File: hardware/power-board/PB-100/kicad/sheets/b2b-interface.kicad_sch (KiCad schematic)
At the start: 1 part

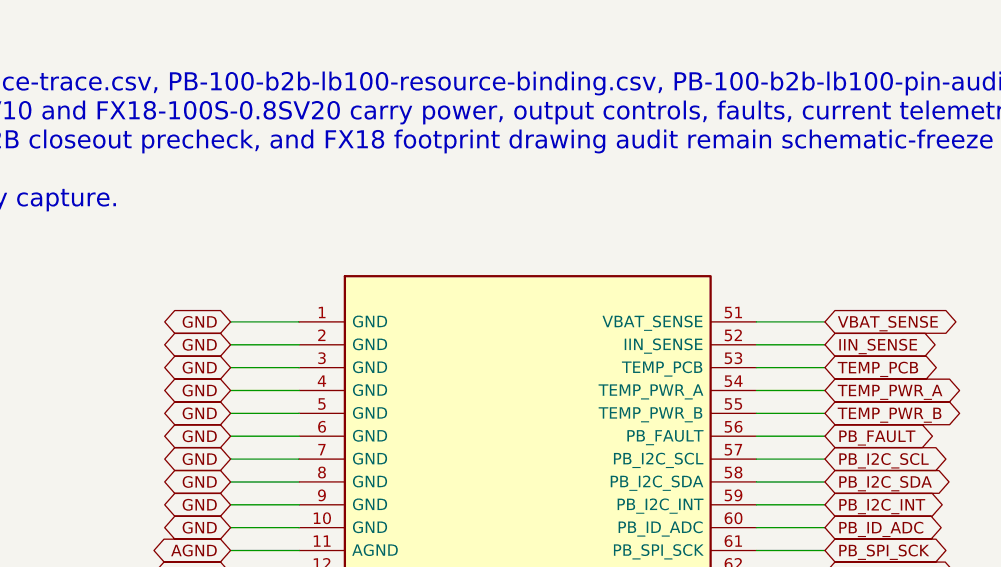
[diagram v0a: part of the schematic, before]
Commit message: feat(hardware): accept CAN1 and 80V freeze decisions
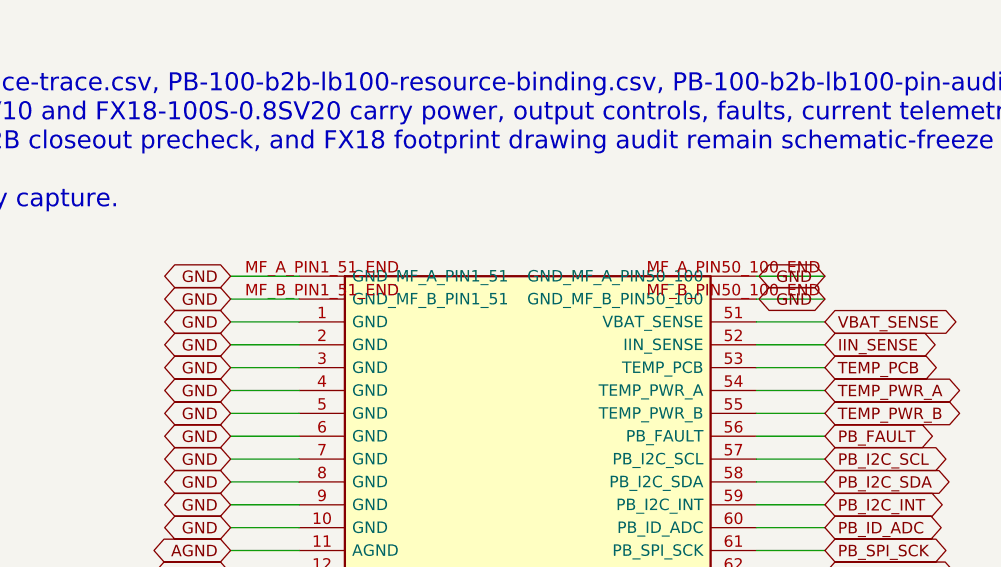
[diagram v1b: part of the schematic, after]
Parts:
- JPB1: footprint (none) -> PB100:FX18-100P-0.8SV10_Hirose
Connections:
- net GND: now also JPB1.MF_A_PIN1_51_END (GND_MF_A_PIN1_51), JPB1.MF_A_PIN50_100_END (GND_MF_A_PIN50_100), JPB1.MF_B_PIN1_51_END (GND_MF_B_PIN1_51), JPB1.MF_B_PIN50_100_END (GND_MF_B_PIN50_100)
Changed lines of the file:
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@@
     (property "Reference" "JPB1" (at 127.00 106.68 0) (effects (font (size 1.27 1.27))))
     (property "Value" "JPB1_100PIN_PRELIM" (at 127.00 109.22 0) (effects (font (size 1.27 1.27))))
-    (property "Footprint" "" (at 127.00 121.92 0) (effects (font (size 1.27 1.27)) hide))
+    (property "Footprint" "PB100:FX18-100P-0.8SV10_Hirose" (at 127.00 121.92 0) (effects (font (size 1.27 1.27)) hide))
     (property "Datasheet" "../PB-100-schematic-capture-plan.md" (at 127.00 124.46 0) (effects (font (size 1.27 1.27)) hide))
     (pin "1")
@@
     (pin "99")
     (pin "100")
+    (pin "MF_A_PIN1_51_END")
+    (pin "MF_B_PIN1_51_END")
+    (pin "MF_A_PIN50_100_END")
+    (pin "MF_B_PIN50_100_END")
     (instances
       (project "PB-100"
@@
     )
   )
+  (wire (pts (xy 101.60 45.72) (xy 93.98 45.72)) (stroke (width 0) (type default)))
+  (global_label "GND" (shape bidirectional) (at 93.98 45.72 0) (fields_autoplaced) (effects (font (size 1.27 1.27)) (justify right)) (property "Intersheetrefs" "${INTERSHEET_REFS}" (at 93.98 45.72 0) (effects (font (size 1.27 1.27)) hide)))
+  (wire (pts (xy 101.60 48.26) (xy 93.98 48.26)) (stroke (width 0) (type default)))
+  (global_label "GND" (shape bidirectional) (at 93.98 48.26 0) (fields_autoplaced) (effects (font (size 1.27 1.27)) (justify right)) (property "Intersheetrefs" "${INTERSHEET_REFS}" (at 93.98 48.26 0) (effects (font (size 1.27 1.27)) hide)))
+  (wire (pts (xy 152.40 45.72) (xy 160.02 45.72)) (stroke (width 0) (type default)))
+  (global_label "GND" (shape bidirectional) (at 160.02 45.72 180) (fields_autoplaced) (effects (font (size 1.27 1.27)) (justify right)) (property "Intersheetrefs" "${INTERSHEET_REFS}" (at 160.02 45.72 0) (effects (font (size 1.27 1.27)) hide)))
+  (wire (pts (xy 152.40 48.26) (xy 160.02 48.26)) (stroke (width 0) (type default)))
+  (global_label "GND" (shape bidirectional) (at 160.02 48.26 180) (fields_autoplaced) (effects (font (size 1.27 1.27)) (justify right)) (property "Intersheetrefs" "${INTERSHEET_REFS}" (at 160.02 48.26 0) (effects (font (size 1.27 1.27)) hide)))
   (wire (pts (xy 101.60 50.80) (xy 93.98 50.80)) (stroke (width 0) (type default)))
   (global_label "GND" (shape bidirectional) (at 93.98 50.80 0) (fields_autoplaced) (effects (font (size 1.27 1.27)) (justify right)) (property "Intersheetrefs" "${INTERSHEET_REFS}" (at 93.98 50.80 0) (effects (font (size 1.27 1.27)) hide)))

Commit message: feat(hardware): close LB FB schematics and FX18 mechanics
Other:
- note added: "B2B interface capture notes: - Source traces: PB-100-b2b-interface-trace.csv, PB-100-b2b-lb100-resource-binding.csv, PB-100-b2b-lb100-pin-audit-checklist.csv, PB-100-b2b-interface-freeze-checklist.csv, PB-100-b2b-interface-closeout-precheck.csv, PB-100-b2b-pin-map.csv, PB-100-b2b-pin-budget.csv - JPB1 candidates FX18-100P-0.8SV10 and FX18-100S-0.8SV10 carry power, output controls, faults, current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"
- note removed: "B2B interface capture notes: - Source traces: PB-100-b2b-interface-trace.csv, PB-100-b2b-lb100-resource-binding.csv, PB-100-b2b-lb100-pin-audit-checklist.csv, PB-100-b2b-interface-freeze-checklist.csv, PB-100-b2b-interface-closeout-precheck.csv, PB-100-b2b-pin-map.csv, PB-100-b2b-pin-budget.csv - JPB1 candidates FX18-100P-0.8SV10 and FX18-100S-0.8SV20 carry power, output controls, faults, current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"
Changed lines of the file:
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@@
     (comment 2 "Sources: PB-100-b2b-interface-trace.csv, PB-100-b2b-lb100-resource-binding.csv, PB-100-b2b-lb100-pin-audit-checklist.csv, PB-100-b2b-interface-freeze-checklist.csv, PB-100-b2b-interface-closeout-precheck.csv, and PB-100-b2b-pin-map.csv.")
   )
-  (text "B2B interface capture notes:\n- Source traces: PB-100-b2b-interface-trace.csv, PB-100-b2b-lb100-resource-binding.csv, PB-100-b2b-lb100-pin-audit-checklist.csv, PB-100-b2b-interface-freeze-checklist.csv, PB-100-b2b-interface-closeout-precheck.csv, PB-100-b2b-pin-map.csv, PB-100-b2b-pin-budget.csv\n- JPB1 candidates FX18-100P-0.8SV10 and FX18-100S-0.8SV20 carry power, output controls, faults, current telemetry, board telemetry, CAN1 safety, and reserves\n- Exact LB-100 MCU pin binding, B2B closeout precheck, and FX18 footprint drawing audit remain schematic-freeze work\n\nNo PCB layout from this preliminary capture."
+  (text "B2B interface capture notes:\n- Source traces: PB-100-b2b-interface-trace.csv, PB-100-b2b-lb100-resource-binding.csv, PB-100-b2b-lb100-pin-audit-checklist.csv, PB-100-b2b-interface-freeze-checklist.csv, PB-100-b2b-interface-closeout-precheck.csv, PB-100-b2b-pin-map.csv, PB-100-b2b-pin-budget.csv\n- JPB1 candidates FX18-100P-0.8SV10 and FX18-100S-0.8SV10 carry power, output controls, faults, current telemetry, board telemetry, CAN1 safety, and reserves\n- Exact LB-100 MCU pin binding, B2B closeout precheck, and FX18 footprint drawing audit remain schematic-freeze work\n\nNo PCB layout from this preliminary capture."
     (at 20 20 0)
     (effects (font (size 2.0 2.0)) (justify left top))

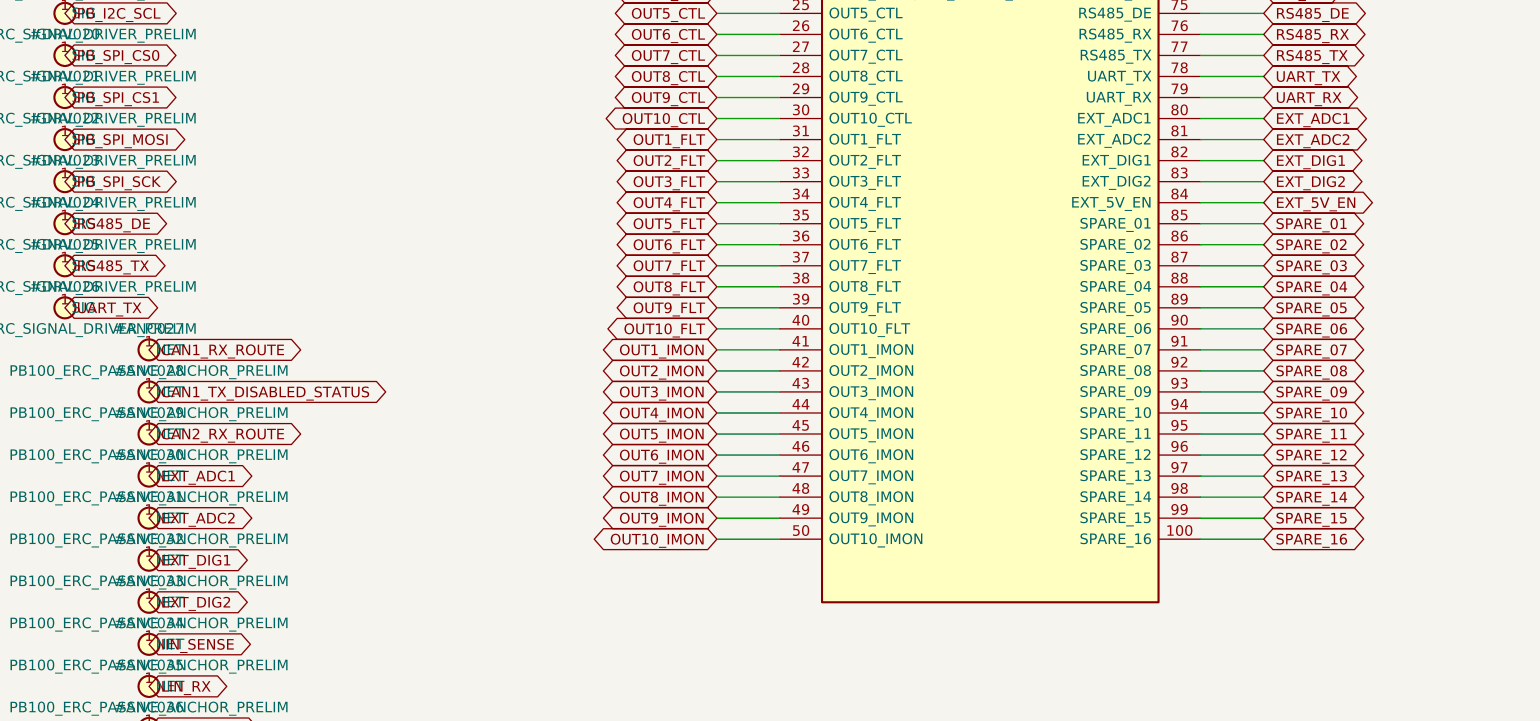
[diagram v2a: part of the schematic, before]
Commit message: feat(platform): authorize unified EVT development
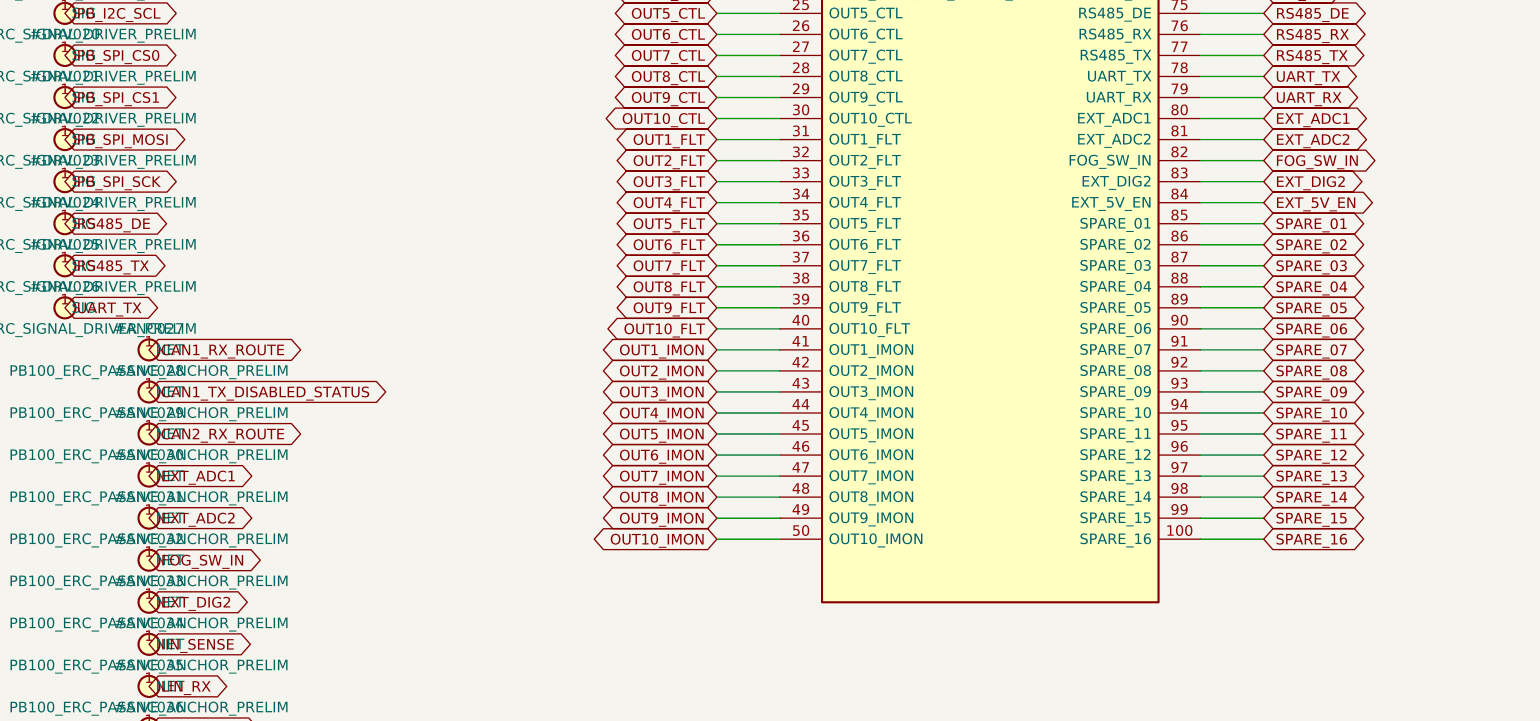
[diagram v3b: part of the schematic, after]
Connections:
- net EXT_DIG1 renamed FOG_SW_IN
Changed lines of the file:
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@@
   (global_label "EXT_ADC2" (shape bidirectional) (at 160.02 127.00 0) (fields_autoplaced) (effects (font (size 1.27 1.27)) (justify left)) (property "Intersheetrefs" "${INTERSHEET_REFS}" (at 160.02 127.00 0) (effects (font (size 1.27 1.27)) hide)))
   (wire (pts (xy 152.40 129.54) (xy 160.02 129.54)) (stroke (width 0) (type default)))
-  (global_label "EXT_DIG1" (shape bidirectional) (at 160.02 129.54 0) (fields_autoplaced) (effects (font (size 1.27 1.27)) (justify left)) (property "Intersheetrefs" "${INTERSHEET_REFS}" (at 160.02 129.54 0) (effects (font (size 1.27 1.27)) hide)))
+  (global_label "FOG_SW_IN" (shape bidirectional) (at 160.02 129.54 0) (fields_autoplaced) (effects (font (size 1.27 1.27)) (justify left)) (property "Intersheetrefs" "${INTERSHEET_REFS}" (at 160.02 129.54 0) (effects (font (size 1.27 1.27)) hide)))
   (wire (pts (xy 152.40 132.08) (xy 160.02 132.08)) (stroke (width 0) (type default)))
   (global_label "EXT_DIG2" (shape bidirectional) (at 160.02 132.08 0) (fields_autoplaced) (effects (font (size 1.27 1.27)) (justify left)) (property "Intersheetrefs" "${INTERSHEET_REFS}" (at 160.02 132.08 0) (effects (font (size 1.27 1.27)) hide)))
@@
     (pin "1")
   )
-  (global_label "EXT_DIG1" (shape bidirectional) (at 25.40 177.80 0) (fields_autoplaced) (effects (font (size 1.27 1.27)) (justify left)) (property "Intersheetrefs" "${INTERSHEET_REFS}" (at 25.40 177.80 0) (effects (font (size 1.27 1.27)) hide)))
-  (symbol
-    (lib_id "PB100:PB100_ERC_PASSIVE_ANCHOR_PRELIM")
+  (global_label "FOG_SW_IN" (shape bidirectional) (at 25.40 177.80 0) (fields_autoplaced) (effects (font (size 1.27 1.27)) (justify left)) (property "Intersheetrefs" "${INTERSHEET_REFS}" (at 25.40 177.80 0) (effects (font (size 1.27 1.27)) hide)))
+  (symbol
+    (lib_id "PB100:PB100_ERC_PASSIVE_ANCHOR_PRELIM")

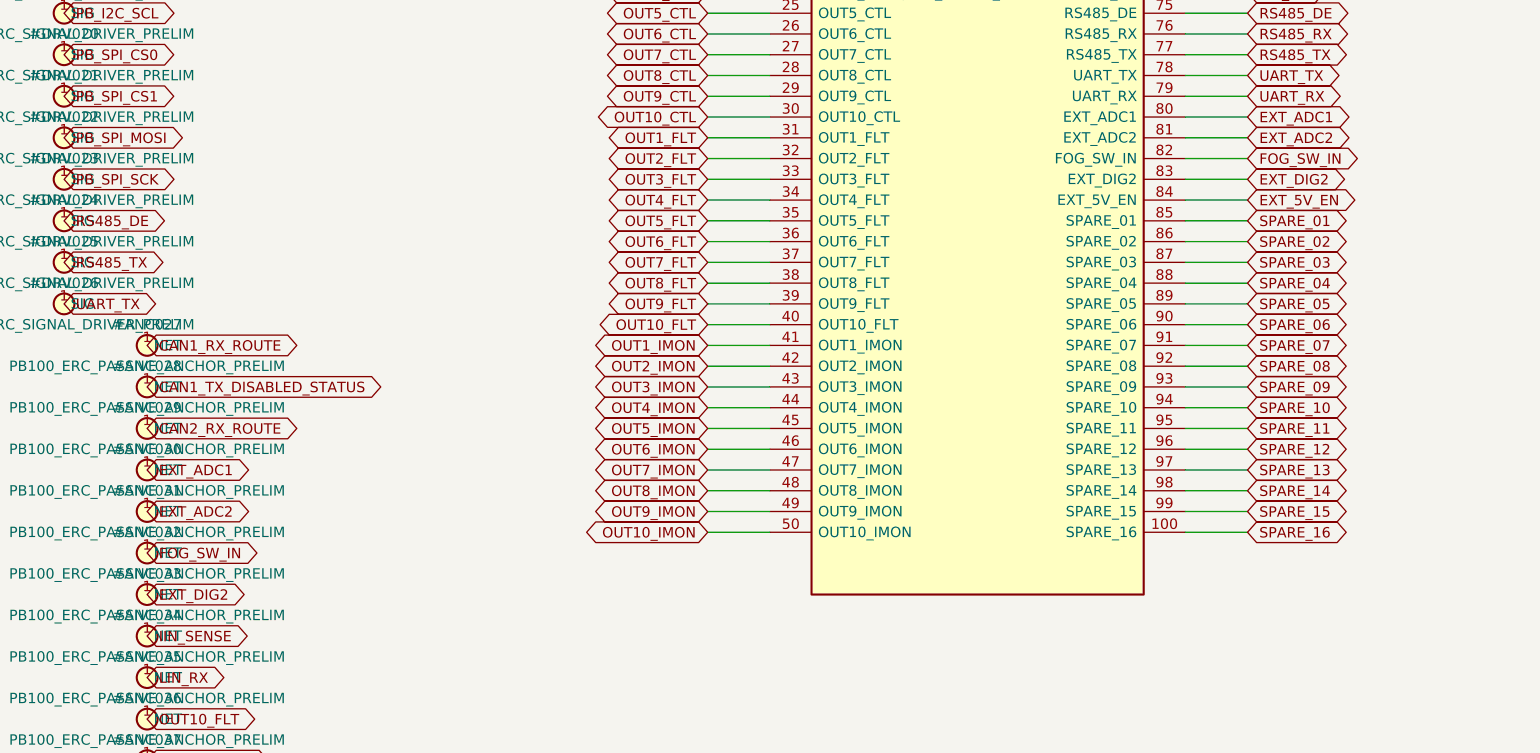
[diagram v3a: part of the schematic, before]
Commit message: feat: add dual protected fog switch inputs
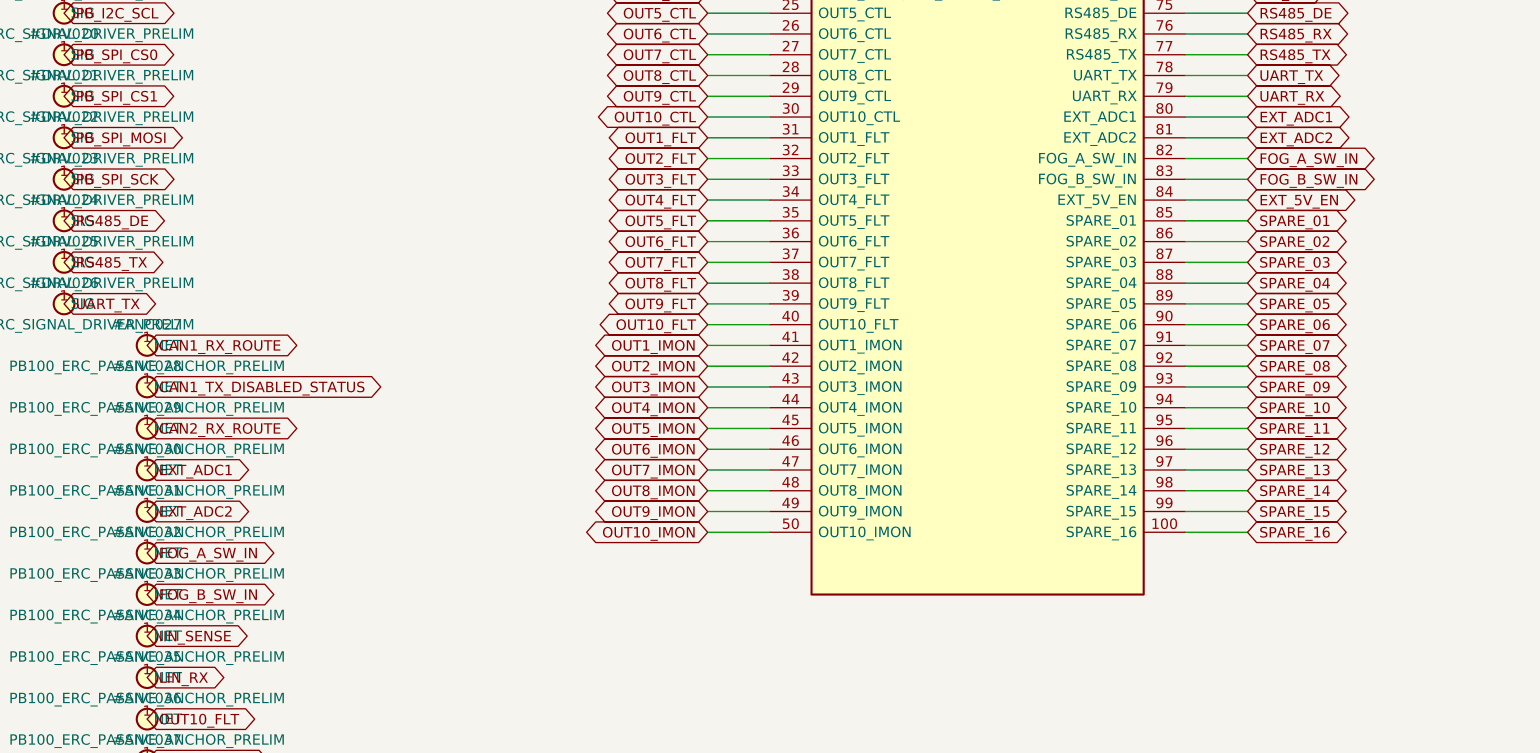
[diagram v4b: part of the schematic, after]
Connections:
- net EXT_DIG2 renamed FOG_B_SW_IN
- net FOG_SW_IN renamed FOG_A_SW_IN
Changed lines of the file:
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@@
   (global_label "EXT_ADC2" (shape bidirectional) (at 160.02 127.00 0) (fields_autoplaced) (effects (font (size 1.27 1.27)) (justify left)) (property "Intersheetrefs" "${INTERSHEET_REFS}" (at 160.02 127.00 0) (effects (font (size 1.27 1.27)) hide)))
   (wire (pts (xy 152.40 129.54) (xy 160.02 129.54)) (stroke (width 0) (type default)))
-  (global_label "FOG_SW_IN" (shape bidirectional) (at 160.02 129.54 0) (fields_autoplaced) (effects (font (size 1.27 1.27)) (justify left)) (property "Intersheetrefs" "${INTERSHEET_REFS}" (at 160.02 129.54 0) (effects (font (size 1.27 1.27)) hide)))
+  (global_label "FOG_A_SW_IN" (shape bidirectional) (at 160.02 129.54 0) (fields_autoplaced) (effects (font (size 1.27 1.27)) (justify left)) (property "Intersheetrefs" "${INTERSHEET_REFS}" (at 160.02 129.54 0) (effects (font (size 1.27 1.27)) hide)))
   (wire (pts (xy 152.40 132.08) (xy 160.02 132.08)) (stroke (width 0) (type default)))
-  (global_label "EXT_DIG2" (shape bidirectional) (at 160.02 132.08 0) (fields_autoplaced) (effects (font (size 1.27 1.27)) (justify left)) (property "Intersheetrefs" "${INTERSHEET_REFS}" (at 160.02 132.08 0) (effects (font (size 1.27 1.27)) hide)))
+  (global_label "FOG_B_SW_IN" (shape bidirectional) (at 160.02 132.08 0) (fields_autoplaced) (effects (font (size 1.27 1.27)) (justify left)) (property "Intersheetrefs" "${INTERSHEET_REFS}" (at 160.02 132.08 0) (effects (font (size 1.27 1.27)) hide)))
   (wire (pts (xy 152.40 134.62) (xy 160.02 134.62)) (stroke (width 0) (type default)))
   (global_label "EXT_5V_EN" (shape bidirectional) (at 160.02 134.62 0) (fields_autoplaced) (effects (font (size 1.27 1.27)) (justify left)) (property "Intersheetrefs" "${INTERSHEET_REFS}" (at 160.02 134.62 0) (effects (font (size 1.27 1.27)) hide)))
@@
     (pin "1")
   )
-  (global_label "FOG_SW_IN" (shape bidirectional) (at 25.40 177.80 0) (fields_autoplaced) (effects (font (size 1.27 1.27)) (justify left)) (property "Intersheetrefs" "${INTERSHEET_REFS}" (at 25.40 177.80 0) (effects (font (size 1.27 1.27)) hide)))
+  (global_label "FOG_A_SW_IN" (shape bidirectional) (at 25.40 177.80 0) (fields_autoplaced) (effects (font (size 1.27 1.27)) (justify left)) (property "Intersheetrefs" "${INTERSHEET_REFS}" (at 25.40 177.80 0) (effects (font (size 1.27 1.27)) hide)))
   (symbol
     (lib_id "PB100:PB100_ERC_PASSIVE_ANCHOR_PRELIM")
@@
     (pin "1")
   )
-  (global_label "EXT_DIG2" (shape bidirectional) (at 25.40 182.88 0) (fields_autoplaced) (effects (font (size 1.27 1.27)) (justify left)) (property "Intersheetrefs" "${INTERSHEET_REFS}" (at 25.40 182.88 0) (effects (font (size 1.27 1.27)) hide)))
-  (symbol
-    (lib_id "PB100:PB100_ERC_PASSIVE_ANCHOR_PRELIM")
+  (global_label "FOG_B_SW_IN" (shape bidirectional) (at 25.40 182.88 0) (fields_autoplaced) (effects (font (size 1.27 1.27)) (justify left)) (property "Intersheetrefs" "${INTERSHEET_REFS}" (at 25.40 182.88 0) (effects (font (size 1.27 1.27)) hide)))
+  (symbol
+    (lib_id "PB100:PB100_ERC_PASSIVE_ANCHOR_PRELIM")
